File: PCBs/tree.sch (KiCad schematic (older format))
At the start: 31 parts, among them J1 Conn_01x06_Female, SW1 SW_Push_DPDT, SW2 SW_SPST, U1 Shift_Reg, U2 Shift_Reg, U3 Shift_Reg, U4 pic18f45k20

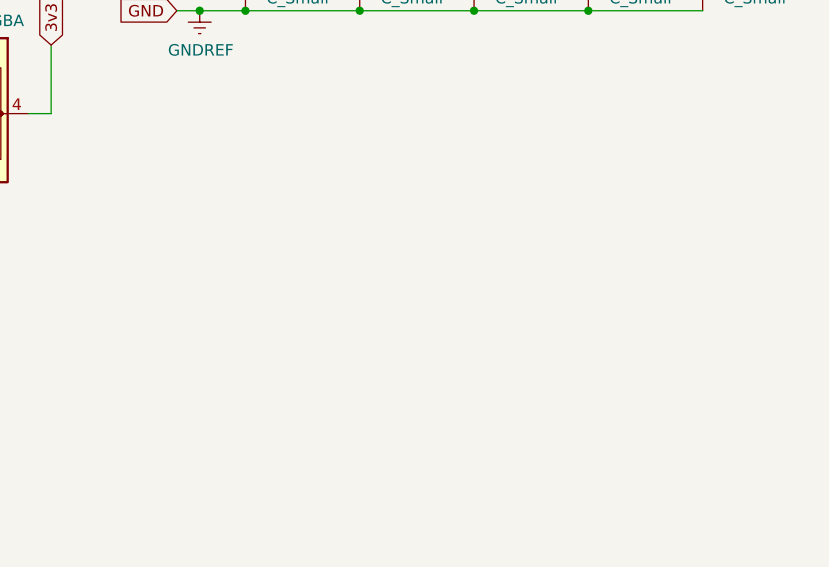
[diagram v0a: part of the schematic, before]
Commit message: Added J2 for a debug/Logic probe header
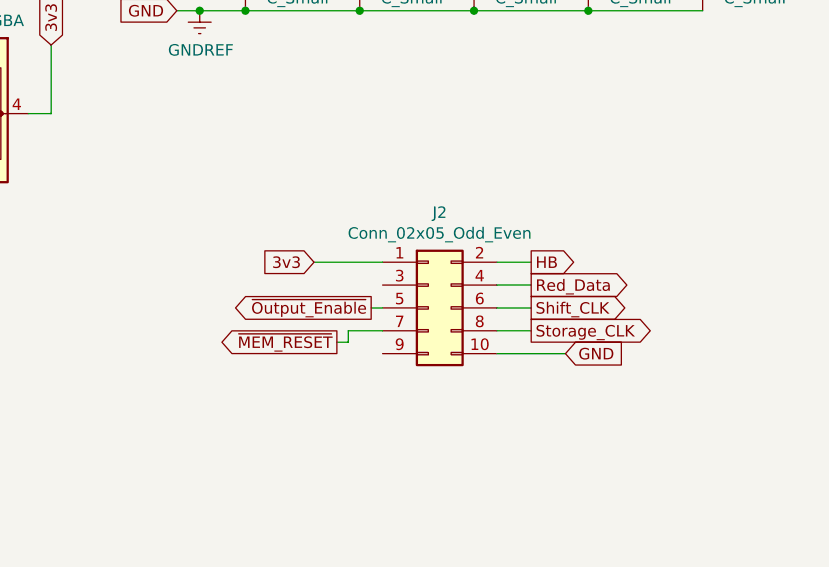
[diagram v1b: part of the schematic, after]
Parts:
- added J2: Conn_02x05_Odd_Even, Connector_PinHeader_2.54mm:PinHeader_2x05_P2.54mm_Vertical, symbol Connector_Generic:Conn_02x05_Odd_Even
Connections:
- net 3v3: now also J2.1 (Pin_1)
- net GNDREF: now also J2.10 (Pin_10)
- net HB: now also J2.2 (Pin_2)
- net Red_Data: now also J2.4 (Pin_4)
- net Shift_CLK: now also J2.6 (Pin_6)
- net Storage_CLK: now also J2.8 (Pin_8)
- net ~MEM_RESET~: now also J2.7 (Pin_7)
- net ~Output_Enable~: now also J2.5 (Pin_5)
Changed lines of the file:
@@
 Text GLabel 8350 2550 0    50   Output ~ 0
 ~MEM_RESET~
+$Comp
+L Connector_Generic:Conn_02x05_Odd_Even J2
+U 1 1 60231BAE
+P 9300 5800
+F 0 "J2" H 9350 6217 50  0000 C CNN
+F 1 "Conn_02x05_Odd_Even" H 9350 6126 50  0000 C CNN
+F 2 "Connector_PinHeader_2.54mm:PinHeader_2x05_P2.54mm_Vertical" H 9300 5800 50  0001 C CNN
+F 3 "~" H 9300 5800 50  0001 C CNN
+	1    9300 5800
+	1    0    0    -1
+$EndComp
+Text GLabel 9050 5800 0    50   Output ~ 0
+~Output_Enable~
+Wire Wire Line
+	9050 5800 9100 5800
+Wire Wire Line
+	8950 5900 9100 5900
+Wire Wire Line
+	8950 5950 8950 5900
+Wire Wire Line
+	8900 5950 8950 5950
+Text GLabel 8900 5950 0    50   Output ~ 0
+~MEM_RESET~
+Text GLabel 9750 5800 2    50   Output ~ 0
+Shift_CLK
+Wire Wire Line
+	9750 5800 9600 5800
+Text GLabel 9750 5900 2    50   Output ~ 0
+Storage_CLK
+Wire Wire Line
+	9750 5900 9600 5900
+Text GLabel 9750 5700 2    50   Output ~ 0
+Red_Data
+Wire Wire Line
+	9750 5700 9600 5700
+Text GLabel 9750 5600 2    50   Output ~ 0
+HB
+Wire Wire Line
+	9750 5600 9600 5600
+Text GLabel 9900 6000 2    50   Input ~ 0
+GND
+Wire Wire Line
+	9900 6000 9600 6000
+Text GLabel 8800 5600 0    50   Input ~ 0
+3v3
+Wire Wire Line
+	8800 5600 9100 5600
 $EndSCHEMATC
